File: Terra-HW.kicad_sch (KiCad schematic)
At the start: 7 parts

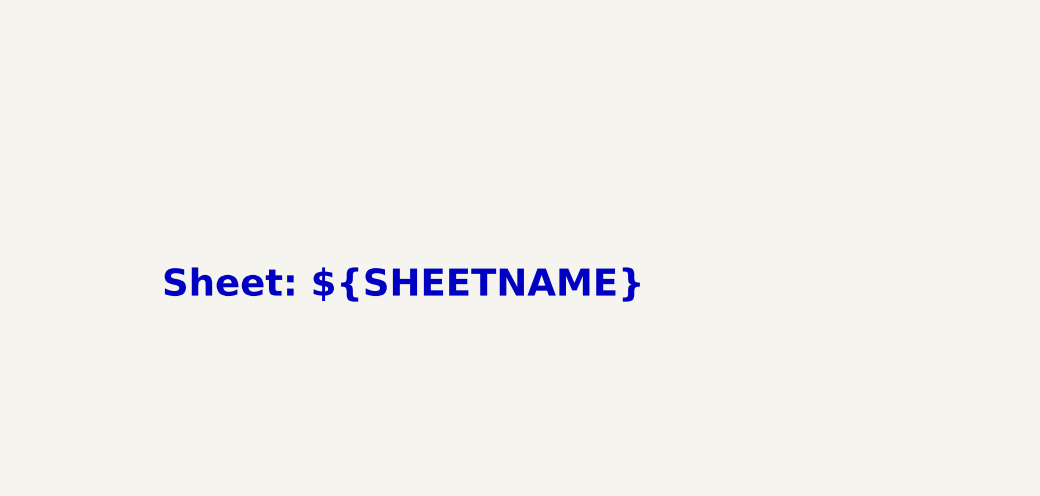
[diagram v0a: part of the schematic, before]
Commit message: Release X01-003 - Added "JRM" logo to L3 and and Modem Works logo to L4. - Upated copyright - Added alternates for some components - Some cleanup on SCH and PCB.
Signed-off-by: James Mendel <jrm.mendel@gmail.com>
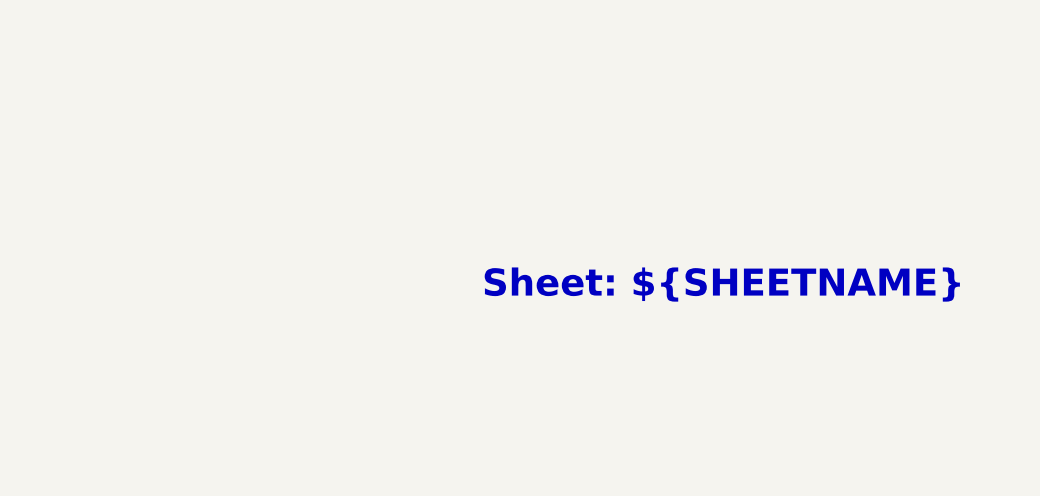
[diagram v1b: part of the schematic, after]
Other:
- company: J. MENDEL -> ${COMPANY}
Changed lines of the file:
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@@
 	(title_block
 		(title "${TITLE}")
-		(date "2025-04-05")
+		(date "2025-04-06")
 		(rev "${REVISION}")
-		(company "J. MENDEL")
+		(company "${COMPANY}")
+		(comment 1 "${LICENSE}")
+		(comment 2 "${COPYRIGHT}")
 	)
 	(text "HAPTICS"
@@
 	(text_box "Sheet: ${SHEETNAME}"
 		(exclude_from_sim no)
-		(at 177.8 167.64 0)
-		(size 106.68 12.7)
+		(at 213.36 167.64 0)
+		(size 71.12 12.7)
 		(margins 0.9525 0.9525 0.9525 0.9525)
 		(stroke
@@
 			"AAAAALEUhAoAAAAAEt+WBQAAAAD4AwAAAAAAADllhAoAAAAAd82WBQAAAAD5AwAAAAAAAFm2hAoA"
 			"AAAAxL+WBQAAAAD6AwAAAAAAAPEHhQoAAAAA+7WWBQAAAAD7AwAAAAAAANRZhQoAAAAAHbCWBQAA"
-			"AAD8AwAAAAAAAOGrhQoAAAAAKa6WBQAAAAD9AwAAAAAAAAAAAA=="
-		)
-	)
+			"AAD8AwAAAAAAAOGrhQoAAAAAKa6WBQAAAAD9AwAAAAAAAAAAAABHCQAAQwkAAEIJAABKCQAARgkA"
+			"AEgJAABKCQAARAkAAEYJAABLCQAASgkAAEgJAABLCQAASAkAAEcJAABMCQAAPQkAADsJAABNCQAA"
+			"PQkAAEwJAABNCQAATgkAAD0JAABPCQAATgkAAE0JAABPCQAAUAkAAE4JAABRCQAAUAkAAE8JAABR"
+			"CQAAUgkAAFAJAABTCQAAUgkAAFEJAABUCQAAUgkAAFMJAABVCQAAUwkAAFYJAABVCQAAVAkAAFMJ"
+			"AABXCQAAVgkAAFgJAABXCQAAVQkAAFYJAABZCQAAWAkAAFoJAABZCQAAVwkAAFgJAABbCQAAWQkA"
+			"AFoJAABbCQAAXAkAAFkJAABdCQAAXAkAAFsJAABdCQAAXgkAAF8JAABdCQAAXwkAAFwJAABgCQAA"
+			"XgkAAF0JAABhCQAAYgkAAF4JAABhCQAAXgkAAGAJAABjCQAAZAkAAGIJAABjCQAAYgkAAGEJAABl"
+			"CQAAZgkAAGcJAABlCQAAaAkAAGYJAABpCQAAagkAAGsJAABpCQAAawkAAGwJAABtCQAAbAkAAG4J"
+			"AABtCQAAaQkAAGwJAABvCQAAbgkAAHAJAABvCQAAbQkAAG4JAABxCQAAcAkAAHIJAABxCQAAbwkA"
+			"AHAJAABzCQAAcgkAAHQJAABzCQAAcQkAAHIJAAB1CQAAdgkAAHcJAAB1CQAAeAkAAHYJAAB5CQAA"
+			"egkAAHsJAAB5CQAAewkAAHwJAAB9CQAAfgkAAH8JAAB9CQAAfwkAAIAJAACBCQAAggkAAIMJAACB"
+			"CQAAhAkAAIIJAACFCQAAhgkAAIIJAACFCQAAggkAAIQJAACHCQAAgwkAAIgJAACHCQAAgQkAAIMJ"
+			"AACJCQAAigkAAIYJAACJCQAAhgkAAIUJAACLCQAAjAkAAIoJAACLCQAAigkAAIkJAACNCQAAjgkA"
+			"AI8JAACNCQAAkAkAAI4JAACRCQAAkgkAAJAJAACRCQAAkAkAAI0JAACTCQAAiAkAAJQJAACTCQAA"
+			"hwkAAIgJAACVCQAAkgkAAJEJAACVCQAAlgkAAJIJAACXCQAAlAkAAJgJAACXCQAAkwkAAJQJAACZ"
+			"CQAAmAkAAJoJAACZCQAAmgkAAJYJAACZCQAAlwkAAJgJAACZCQAAlgkAAJUJAACbCQAAnAkAAIwJ"
+			"AACbCQAAjAkAAIsJAACdCQAAnAkAAJsJAACdCQAAngkAAJwJAACfCQAAngkAAJ0JAACfCQAAoAkA"
+			"AJ4JAAChCQAAoAkAAJ8JAAChCQAAogkAAKAJAACjCQAAogkAAKEJAACkCQAAogkAAKMJAAClCQAA"
+			"owkAAKYJAAClCQAApAkAAKMJAACnCQAApQkAAKYJAACoCQAApQAAAAAAAAAAAAAAAAAAAAAAAAAA"
+			"AAAAAAAAAAAAAAAAAAAAAAAAAAAAAAAAAAAAAAAAAAAAAAAAAAAAAAAAAAAAAAAAAAAAAAAAAAAA"
+			"AAAAAAAAAAAAAAAAAAAAAAAAAAAAAAAAAAAAAAAAAAAAAAAAAAAAAAAAAAAAAAAAAAAAAAAAAAAA"
+			"AAAAAAAAAAAAAAAAAAAAAAAAAAAAAAAAAAAAAAAAAAAAAAAAAAAAAAAAAAAAAAAAAAAAAAAAAAAA"
+			"AAAAAAAAAAAAAAAAAAAAAAAAAAAAAAAAAAAAAAAAAAAAAAAAAAAAAAAAAAAAAAAAAAAAAAAAAAAA"
+			"AAAAAAAAAAAAAAAAAAAAAAAAAAAAAAAAAAAAAAAAAAAAAAAAAAAAAAAAAAAAAAAAAAAAAAAAAAAA"
+			"AAAAAAAAAAAAAAAAAAAAAAAAAAAAAAAAAAAAAAAAAAAAAAAAAAAAAAAAAAAAAAAAAAAAAAAAAAAA"
+			"AAAAAAAAAAAAAAAAAAAAAAAAAAAAAAAAAAAAAAAAAAAAAAAAAAAAAAAAAAAAAAAAAAAAAAAAAAAA"
+			"AAAAAAAAAAAAAAAAAAAAAAAAAAAAAAAAAAAAAAAAAAAAAAAAAAAAAAAAAAAAAAAAAAAAAAAAAAAA"
+			"AAAAAAAAAAAAAAAAAAAAAAAAAAAAAAAAAAAAAAAAAAAAAAAAAAAAAAAAAAAAAAAAAAAAAAAAAAAA"
+			"AAAAAAAAAAAAAAAAAAAAAAAAAAAAAAAAAAAAAAAAAAAAAAAAAAAAAAAAAAAAAAAAAAAAAAAAAAAA"
+			"AAAAAAAAAAAAAAAAAAAAAAAAAAAAAAAAAAAAAAAAAAAAAAAAAAAAAAAAAAAAAAAAAAAAAAAAAAAA"
+			"AAAAAAAAAAAAAAAAAAAAAAAAAAAAAAAAAAAAAAAAAAAAAAAAAAAAAAAAAAAAAAAAAAAAAAAAAAAA"
+			"AAAAAAAAAAAAAAAAAAAAAAAAAAAAAAAAAAAAAAAAAAAAAAAAAAAAAAAAAAAAAAAAAAAAAAAAAAAA"
+			"AAAAAAAAAAAAAAAAAAAAAAAAAAAAAAAAAAAAAAAAAAAAAAAAAAAAAAAAAAAAAAAAAAAAAAAAAAAA"
+			"AAAAAAAAAAAAAAAAAAAAAAAAAAAAAAAAAAAAAAAAAAAAAAAAAAAAAAAAAAAAAAAAAAAAAAAAAAAA"
+			"AAAAAAAAAAAAAAAAAAAAAAAAAAAAAAAAAAAAAAAAAAAAAAAAAAAAAAAAAAAAAAAAAAAAAAAAAAAA"
+			"AAAAAAAAAAAAAAAAAAAAAAAAAAAAAAAAAAAAAAAAAAAAAAAAAAAAAAAAAAAAAAAAAAAAAAAAAAAA"
+			"AAAAAAAAAAAAAAAAAAAAAAAAAAAAAAAAAAAAAAAAAAAAAAAAAA=="
+		)
+	)
